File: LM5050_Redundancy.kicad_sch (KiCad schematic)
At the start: 2 parts, among them Q1 SUM40N10-30, U1 LM5050-1

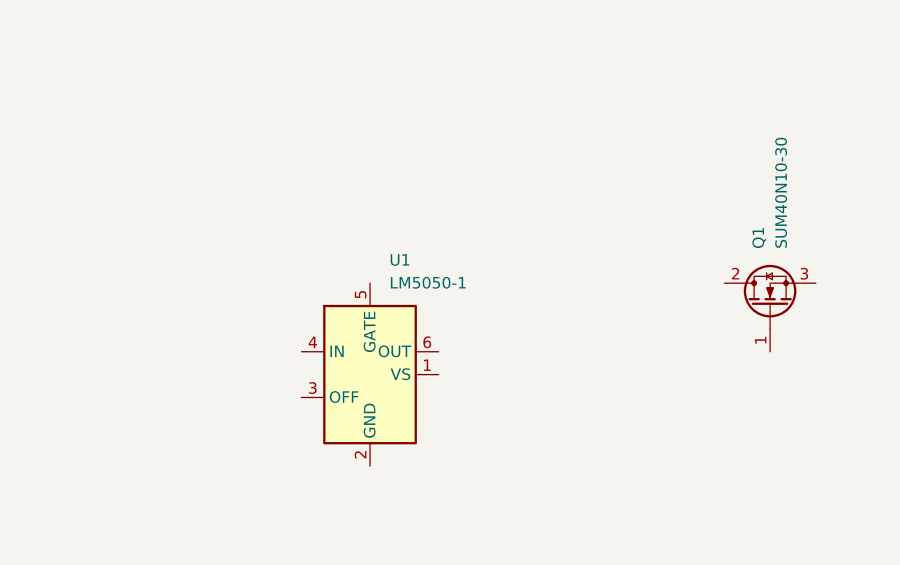
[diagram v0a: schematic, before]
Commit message: create single LM5050 power path
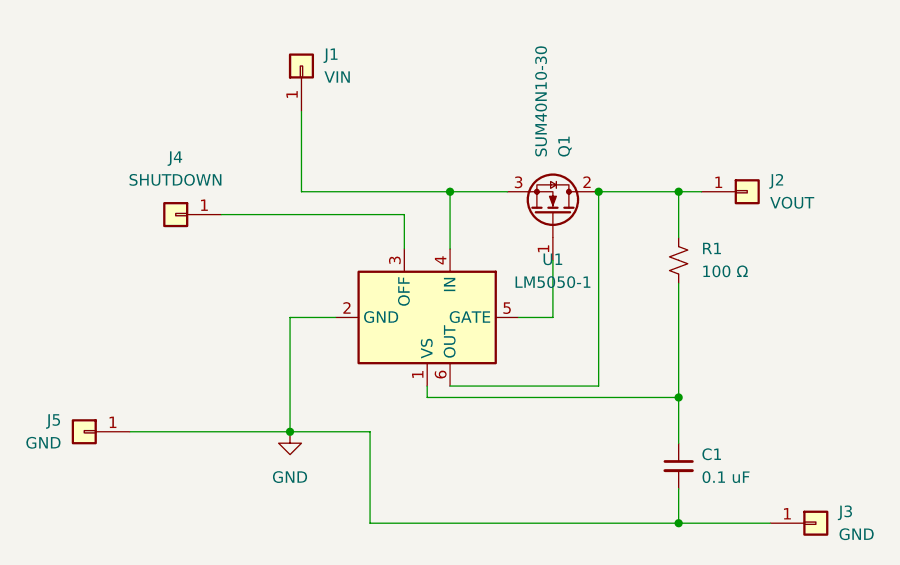
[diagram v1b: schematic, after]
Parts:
- added C1: 0.1 uF, symbol Device:C_Small
- added J1: VIN, symbol Connector_Generic:Conn_01x01
- added J2: VOUT, symbol Connector_Generic:Conn_01x01
- added J3, J5: GND, symbol Connector_Generic:Conn_01x01
- added J4: SHUTDOWN, symbol Connector_Generic:Conn_01x01
- added R1: 100 Ω, symbol Device:R_Small_US
- Q1: footprint (none) -> Package_TO_SOT_SMD:TO-263-3_TabPin2
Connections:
- net at Q1.1 (G): now also U1.5 (GATE)
- net at Q1.2 (D): now also U1.6 (OUT), J2.1 (Pin_1), R1.1
- net at Q1.3 (S): now also U1.4 (IN), J1.1 (Pin_1)
- net at U1.1 (VS): now also C1.1, R1.2
- net GND: now reaches U1.2 (GND)
- net GND: now also C1.2, J3.1 (Pin_1), J5.1 (Pin_1)
- net at U1.3 (OFF): now also J4.1 (Pin_1)
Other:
- moved on the sheet: Q1, U1

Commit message: Assign footprints and ERC
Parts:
- added C2: 0.1 uF, Capacitor_SMD:C_0805_2012Metric, symbol Device:C_Small
- added J10, J6: GND, Connector_PinHeader_2.54mm:PinHeader_1x01_P2.54mm_Vertical, symbol Connector_Generic:Conn_01x01
- added J7: SHUTDOWN, Connector_PinHeader_2.54mm:PinHeader_1x01_P2.54mm_Vertical, symbol Connector_Generic:Conn_01x01
- added J8: VIN2, Connector_PinHeader_2.54mm:PinHeader_1x01_P2.54mm_Vertical, symbol Connector_Generic:Conn_01x01
- added Q2: SUM40N10-30, Package_TO_SOT_SMD:TO-263-3_TabPin2, symbol Transistor_FET:Q_NMOS_GDS
- added R2: 100 Ω, Resistor_SMD:R_0805_2012Metric, symbol Device:R_Small_US
- added U2: LM5050-1, Package_TO_SOT_SMD:TSOT-23-6, symbol Power_Management:LM5050-1
- C1: footprint (none) -> Capacitor_SMD:C_0805_2012Metric
- J1: value VIN -> VIN1; footprint (none) -> Connector_PinHeader_2.54mm:PinHeader_1x01_P2.54mm_Vertical
- J2, J3, J4, J5: footprint (none) -> Connector_PinHeader_2.54mm:PinHeader_1x01_P2.54mm_Vertical
- R1: footprint (none) -> Resistor_SMD:R_0805_2012Metric
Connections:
- net GND: now also C2.2, J10.1 (Pin_1), J6.1 (Pin_1), U2.2 (GND)
- net at J2.1 (Pin_1), Q1.2 (D), R1.1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: now also Q2.2 (D), R2.1, U2.6 (OUT)
- new net: J7.1 (Pin_1), U2.3 (OFF)
- new net: J8.1 (Pin_1), Q2.3 (S), U2.4 (IN)
- new net: Q2.1 (G), U2.5 (GATE)
- new net: C2.1, R2.2, U2.1 (VS)
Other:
- moved on the sheet: J2
